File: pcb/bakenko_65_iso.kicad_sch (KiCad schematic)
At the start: 50 parts, among them J1 JST SH 4-pin, J2 Conn_01x02_MountingPin, K1 BUTTON-4P, Q1 AO3407A, U1 XC6206P302MR-G, U2 NRF52840 aQFN73, U3 MCP73831, X1 32MHz, X2 32.768KHz

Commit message: WIP + Cleaned repository
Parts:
- removed C1, C2: 1uF, Capacitor_SMD:C_0402_1005Metric, symbol Device:C_Small
- removed C11: 100pF, Capacitor_SMD:C_0402_1005Metric, symbol Device:C_Small
- removed C20: 4.7uF, Capacitor_SMD:C_0402_1005Metric, symbol Device:C_Small
- removed C7: 100nF, Capacitor_SMD:C_0402_1005Metric, symbol Device:C_Small
- removed K1: BUTTON-4P, Seeed Studio XIAO nRF52840 v1.1:SW4-SMD-2.8-2.6X1.6X0.53MM, symbol Seeed Studio XIAO nRF52840 v1.1-eagle-import:BUTTON-4P
- removed R4, R5: 33R, Resistor_SMD:R_0402_1005Metric, symbol Seeed Studio XIAO nRF52840 v1.1-eagle-import:R-0201
- added SW1: SW_Omron_B3FS, Button_Switch_SMD:SW_SPST_TS-1088-xR020, symbol Switch:SW_Omron_B3FS
- C11: renamed from C23; value 100nF -> 100pF
- C12: renamed from C29; value C_Small -> 100nF; footprint (none) -> Capacitor_SMD:C_0402_1005Metric
- C14: renamed from C31; value C_Small -> 1uF; footprint (none) -> Capacitor_SMD:C_0603_1608Metric
- C15: renamed from C27; footprint Capacitor_SMD:C_0402_1005Metric -> Capacitor_SMD:C_0603_1608Metric
- C20: renamed from C21; footprint Capacitor_SMD:C_0402_1005Metric -> Capacitor_SMD:C_0603_1608Metric
- C21: renamed from C25; footprint Capacitor_SMD:C_0402_1005Metric -> Capacitor_SMD:C_0603_1608Metric
- C6: renamed from C32; value C_Small -> 4.7uF; footprint (none) -> Capacitor_SMD:C_0603_1608Metric
- C7: renamed from C28; footprint (none) -> Capacitor_SMD:C_0402_1005Metric
- C8: renamed from C30; value C_Small -> 100nF; footprint (none) -> Capacitor_SMD:C_0402_1005Metric
- L1: renamed from C13; symbol Seeed Studio XIAO nRF52840 v1.1-eagle-import:L0201 -> Device:L
- L2: renamed from C15; symbol Seeed Studio XIAO nRF52840 v1.1-eagle-import:L0201 -> Device:L
- L3: renamed from C18; symbol Seeed Studio XIAO nRF52840 v1.1-eagle-import:L0201 -> Device:L
- R1, R10, R2, R3: symbol Seeed Studio XIAO nRF52840 v1.1-eagle-import:R-0201 -> Device:R_Small
- X1: footprint Crystal:Crystal_SMD_Abracon_ABM3C-4Pin_5.0x3.2mm -> Crystal:Crystal_SMD_2016-4Pin_2.0x1.6mm; symbol Device:Crystal_GND24_Small -> Device:Crystal
- X2: footprint Crystal:Crystal_SMD_Abracon_ABS25-4Pin_8.0x3.8mm -> Crystal:Crystal_SMD_3215-2Pin_3.2x1.5mm; symbol Device:Crystal_GND23_Small -> Device:Crystal
- renumbered C6 to C1, C12 to C10, C5 to C13, C9 to C17, C16 to C18, C8 to C2, C17 to C3, C3 to C30, C4 to C31, C14 to C33, C19 to C4, C10 to C5
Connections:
- net +3V3: now also C12.2, C14.2, C30.2, C6.2, C7.2, C8.2, R10.2, U1.2 (VO), U2.A22 (VDD), U2.AD14 (VDD), U2.AD23 (VDD), U2.B1 (VDD), U2.W1 (VDD); no longer C12.1, C14.1, C6.1, C7.1, C8.1
- net COL0: now also U2.A20 (P1.10); no longer U2.H2 (P0.27)
- net COL1: now also U2.A16 (P1.13); no longer U2.K2 (P0.05)
- net COL2: now also U2.A14 (P1.15); no longer U2.T2 (P0.11)
- net COL3: now also U2.A12 (P0.02); no longer U2.P2 (P1.08)
- net COL4: now also U2.A10 (P0.29); no longer U2.M2 (P0.07)
- net GND: now also C12.1, C14.1, C2.1, C3.1, C4.1, C6.1, C7.1, C8.1, R1.2, R12.2, U2.B3 (DCC), U3.2 (V_{SS}), SW1.2; no longer C2.2, R1.1, X1.2 (G), X1.4 (G), X2.2 (G), X2.3 (G)
- net P0.14_~{READ_BAT}: now also U2.AD10 (P0.15); no longer U2.AC9 (P0.14)
- net RESET: now also R10.1, U2.AD12 (P0.17), SW1.1; no longer R10.2
- net ROW0: now also U2.J24 (P0.10); no longer U2.U24 (P1.04)
- net ROW1: now also U2.L24 (P0.09); no longer U2.W24 (P1.02)
- net ROW3: now also U2.U24 (P1.04); no longer U2.L24 (P0.09)
- net ROW4: now also U2.W24 (P1.02); no longer U2.J24 (P0.10)
- net USB_D+: now also U2.AD6 (D+)
- net USB_D-: now also U2.AD4 (D-)
- net VBUS: now also Q1.3 (D), R1.1; no longer Q1.2 (S), R1.2
- net VIN: now also Q1.2 (S); no longer Q1.3 (D)
- net X2_P: now reaches C17.2, U2.D2 (P0.00)
- net X2_P: now also X2.2; no longer X2.4
- net XC_P: now reaches X1.1
- net XC_P: now also C2.2, U2.A23 (XC2); no longer C2.1
- net XC_N: now reaches C1.1
- net XC_N: now also U2.B24 (XC1), X1.2; no longer X1.3
- net X2_N: now reaches C18.2, U2.F2 (P0.01), X2.1
- removed net 3V3: C30.2, R10.1, U1.2 (VO)
- net P1.11_TX_D6: no longer names the net of U2.B19 (P1.11)
- no-connect marks 40 -> 27
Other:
- moved on the sheet: C1, C12, C14, C2, C5, C6, C7, C8, L1, L2, L3, Q1

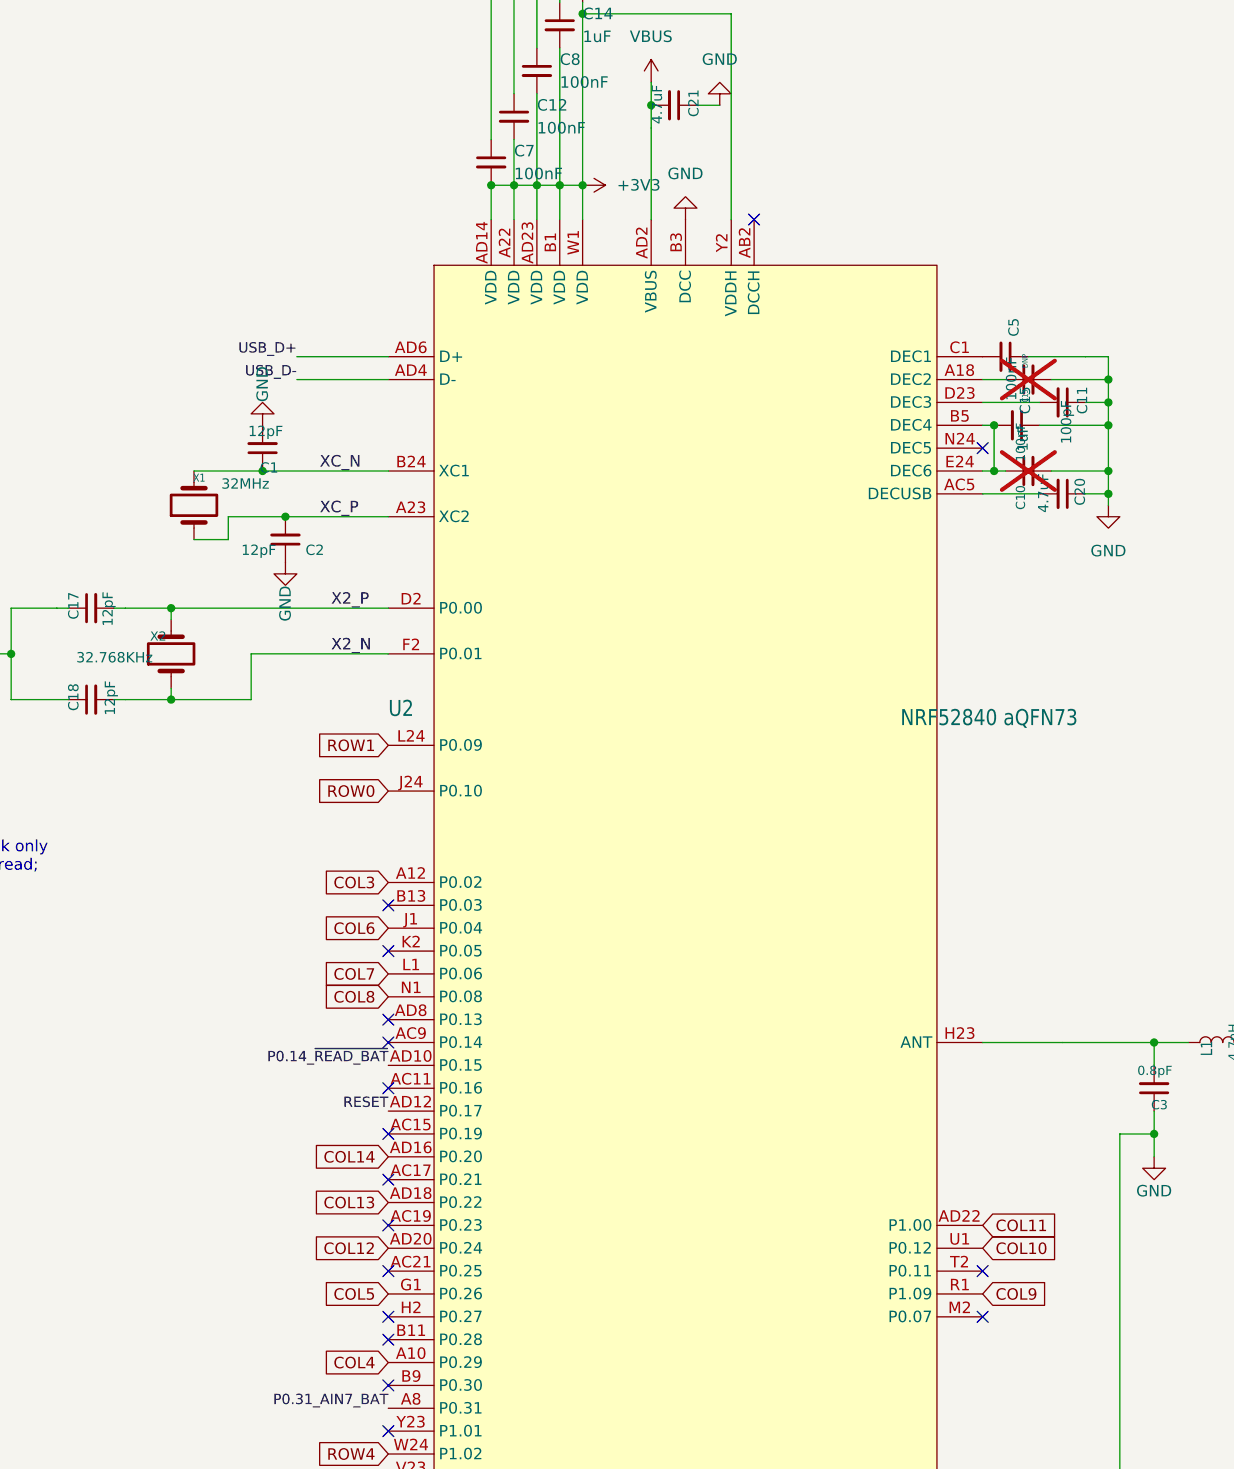
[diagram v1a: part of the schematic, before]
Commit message: 🧹Cleaned more up and updated the readme
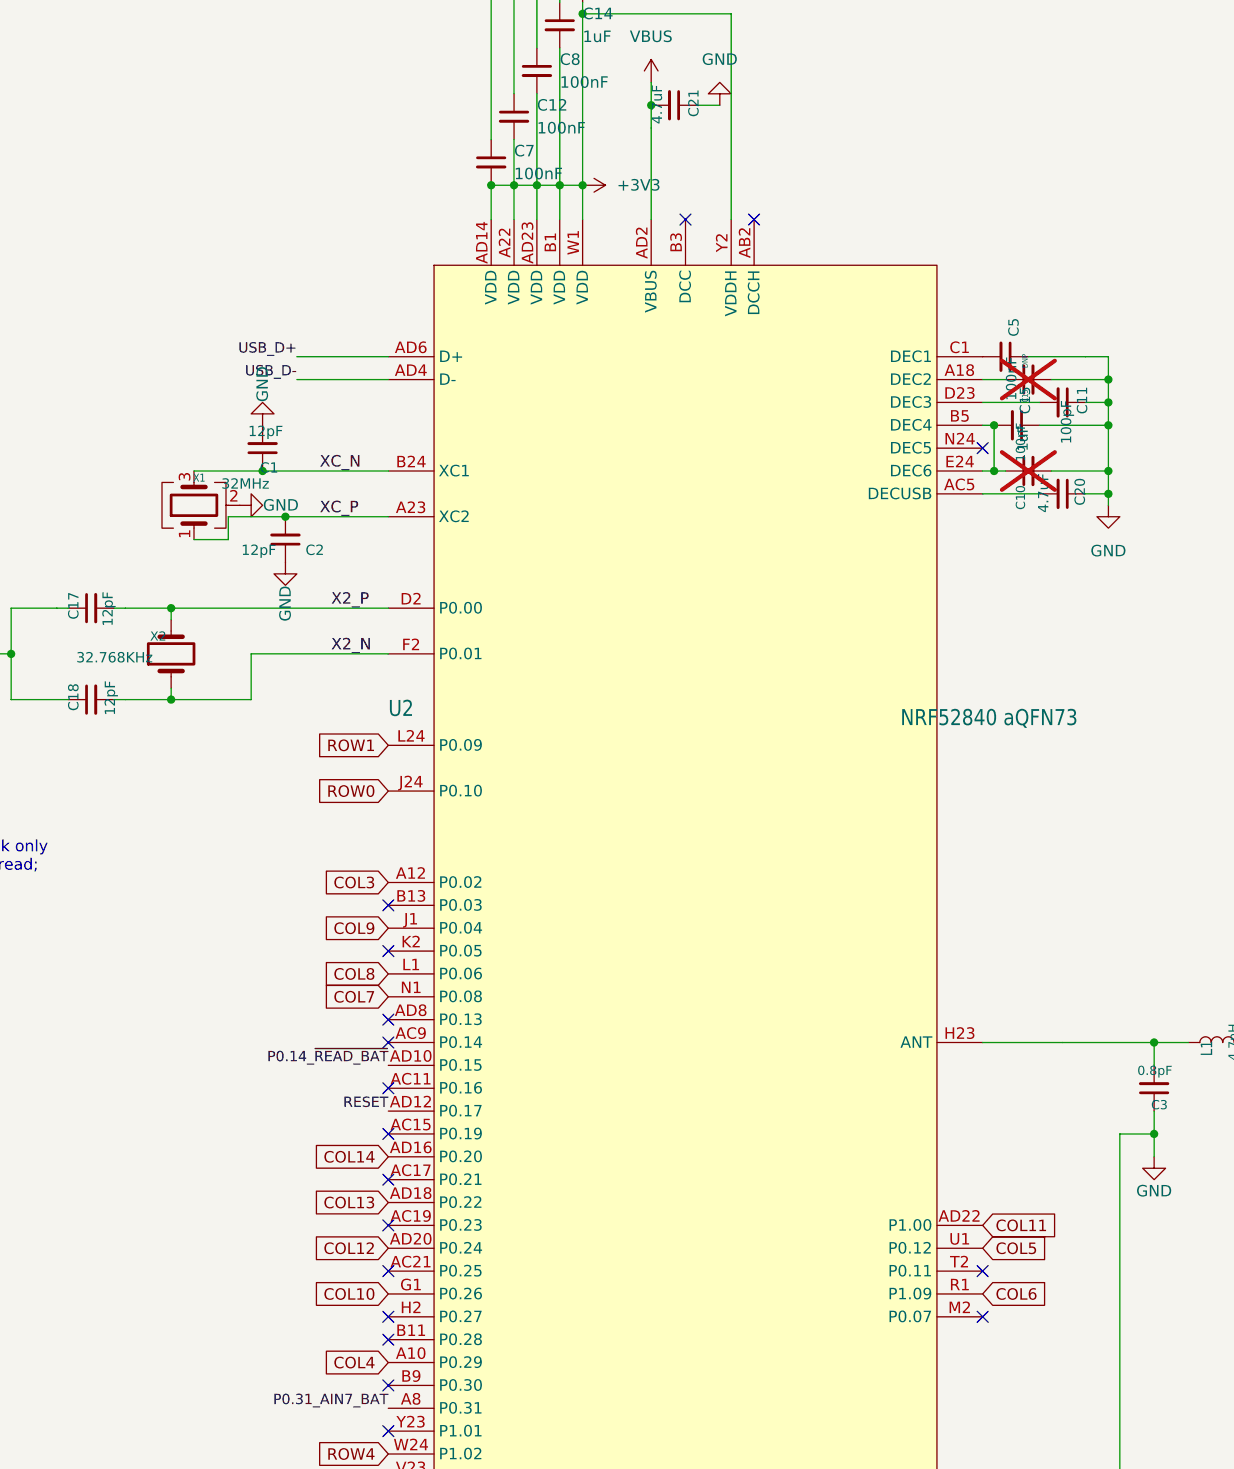
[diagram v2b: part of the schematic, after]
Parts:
- X1: symbol Device:Crystal -> Device:Crystal_GND24
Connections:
- net COL10: now also U2.G1 (P0.26); no longer U2.U1 (P0.12)
- net COL5: now also U2.U1 (P0.12); no longer U2.G1 (P0.26)
- net COL6: now also U2.R1 (P1.09); no longer U2.J1 (P0.04)
- net COL7: now also U2.N1 (P0.08); no longer U2.L1 (P0.06)
- net COL8: now also U2.L1 (P0.06); no longer U2.N1 (P0.08)
- net COL9: now also U2.J1 (P0.04); no longer U2.R1 (P1.09)
- net GND: now also X1.2 (G), X1.4 (G); no longer U2.B3 (DCC)
- net XC_N: now also X1.3; no longer X1.2
- no-connect marks 27 -> 28
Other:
- title: Bakeneko 65 V3 -> Bakeneko 65 V4 ISO
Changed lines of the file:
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@@
 	(paper "A3")
 	(title_block
-		(title "Bakeneko 65 V3")
-		(date "2020-08-01")
-		(rev "1")
-		(comment 1 "Copyright © 2020 kkatano")
-		(comment 2 "MIT License")
+		(title "Bakeneko 65 V4 ISO")
+		(date "2026-04-06")
+		(comment 1 "MIT License")
 	)
 	(text "nRF52840"
@@
 	)
 	(no_connect
+		(at 215.9 92.71)
+	)
+	(no_connect
 		(at 182.88 232.41)
 	)
@@
 		)
 	)
-	(global_label "COL9"
+	(global_label "COL6"
 		(shape input)
 		(at 248.92 212.09 0)
@@
 		)
 	)
-	(global_label "COL8"
+	(global_label "COL7"
 		(shape input)
 		(at 182.88 179.07 180)
@@
 		)
 	)
-	(global_label "COL7"
+	(global_label "COL8"
 		(shape input)
 		(at 182.88 176.53 180)
@@
 		)
 	)
-	(global_label "COL10"
+	(global_label "COL5"
 		(shape input)
 		(at 248.92 207.01 0)
@@
 		)
 	)
-	(global_label "COL6"
+	(global_label "COL9"
 		(shape input)
 		(at 182.88 171.45 180)
@@
 		)
 	)
-	(global_label "COL5"
+	(global_label "COL10"
 		(shape input)
 		(at 182.88 212.09 180)
@@
 	)
 	(symbol
+		(lib_name "GND_26")
+		(lib_id "power:GND")
+		(at 166.37 124.46 90)
+		(unit 1)
+		(body_style 1)
+		(exclude_from_sim no)
+		(in_bom yes)
+		(on_board yes)
+		(in_pos_files yes)
+		(dnp no)
+		(property "Reference" "#PWR034"
+			(at 172.72 124.46 0)
+			(hide yes)
+			(show_name no)
+			(do_not_autoplace no)
+			(effects
+				(font
+					(size 1.27 1.27)
+				)
+			)
+		)
+		(property "Value" "GND"
+			(at 170.942 124.46 90)
+			(show_name no)
+			(do_not_autoplace no)
+			(effects
+				(font
+					(size 1.27 1.27)
+				)
+			)
+		)
+		(property "Footprint" ""
+			(at 166.37 124.46 0)
+			(hide yes)
+			(show_name no)
+			(do_not_autoplace no)
+			(effects
+				(font
+					(size 1.27 1.27)
+				)
+			)
+		)
+		(property "Datasheet" ""
+			(at 166.37 124.46 0)
+			(hide yes)
+			(show_name no)
+			(do_not_autoplace no)
+			(effects
+				(font
+					(size 1.27 1.27)
+				)
+			)
+		)
+		(property "Description" "Power symbol creates a global label with name \"GND\" , ground"
+			(at 166.37 124.46 0)
+			(hide yes)
+			(show_name no)
+			(do_not_autoplace no)
+			(effects
+				(font
+					(size 1.27 1.27)
+				)
+			)
+		)
+		(pin "1"
+		)
+		(instances
+			(project "bakenko_65_iso"
+				(path "/287514b3-fc8e-4781-96ec-6e4b29b57f7d"
+					(reference "#PWR034")
+					(unit 1)
+				)
+			)
+		)
+	)
+	(symbol
 		(lib_id "Regulator_Linear:XC6206PxxxMR")
 		(at 95.25 73.66 0)
@@
 	)
 	(symbol
-		(lib_id "Device:Crystal")
+		(lib_id "Device:Crystal_GND24")
 		(at 161.29 124.46 90)
 		(unit 1)
@@
 			)
 		)
-		(property "Datasheet" ""
+		(property "Datasheet" "https://www.lcsc.com/datasheet/C187794.pdf"
 			(at 161.29 124.46 0)
 			(hide yes)
@@
 			)
 		)
-		(property "Description" "XTAL SMD 2016, 32 MHz, Cl=8 pF, Total Tol: ±40 ppm"
+		(property "Description" "Four pin crystal, GND on pins 2 and 4"
 			(at 161.29 124.46 0)
 			(hide yes)
@@
 		(pin "2"
 		)
+		(pin "4"
+		)
+		(pin "3"
+		)
 		(instances
 			(project "bakenko_65_iso"
@@
 					(unit 1)
 				)
-			)
-		)
-	)
-	(symbol
-		(lib_name "GND_2")
-		(lib_id "power:GND")
-		(at 215.9 92.71 180)
-		(unit 1)
-		(body_style 1)
-		(exclude_from_sim no)
-		(in_bom yes)
-		(on_board yes)
-		(in_pos_files yes)
-		(dnp no)
-		(fields_autoplaced yes)
-		(property "Reference" "#PWR03"
-			(at 215.9 86.36 0)
-			(hide yes)
-			(show_name no)
-			(do_not_autoplace no)
-			(effects
-				(font
-					(size 1.27 1.27)
-				)
-			)
-		)
-		(property "Value" "GND"
-			(at 215.9 87.63 0)
-			(show_name no)
-			(do_not_autoplace no)
-			(effects
-				(font
-					(size 1.27 1.27)
-				)
-			)
-		)
-		(property "Footprint" ""
-			(at 215.9 92.71 0)
-			(hide yes)
-			(show_name no)
-			(do_not_autoplace no)
-			(effects
-				(font
-					(size 1.27 1.27)
-				)
-			)
-		)
-		(property "Datasheet" ""
-			(at 215.9 92.71 0)
-			(hide yes)
-			(show_name no)
-			(do_not_autoplace no)
-			(effects
-				(font
-					(size 1.27 1.27)
-				)
-			)
-		)
-		(property "Description" "Power symbol creates a global label with name \"GND\" , ground"
-			(at 215.9 92.71 0)
-			(hide yes)
-			(show_name no)
-			(do_not_autoplace no)
-			(effects
-				(font
-					(size 1.27 1.27)
-				)
-			)
-		)
-		(pin "1"
-		)
-		(instances
-			(project "bakenko_65_iso"
-				(path "/287514b3-fc8e-4781-96ec-6e4b29b57f7d"
-					(reference "#PWR03")
-					(unit 1)
-				)

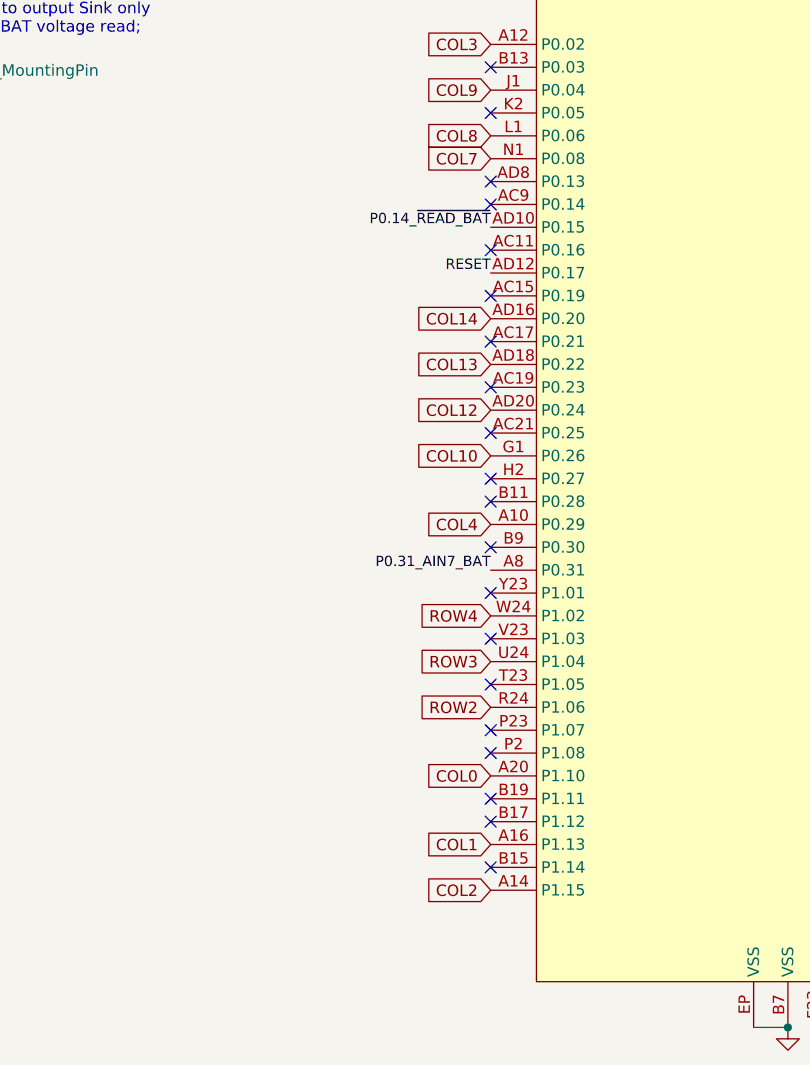
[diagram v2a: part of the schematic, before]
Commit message: Connecting reset and reducing errors and warnings
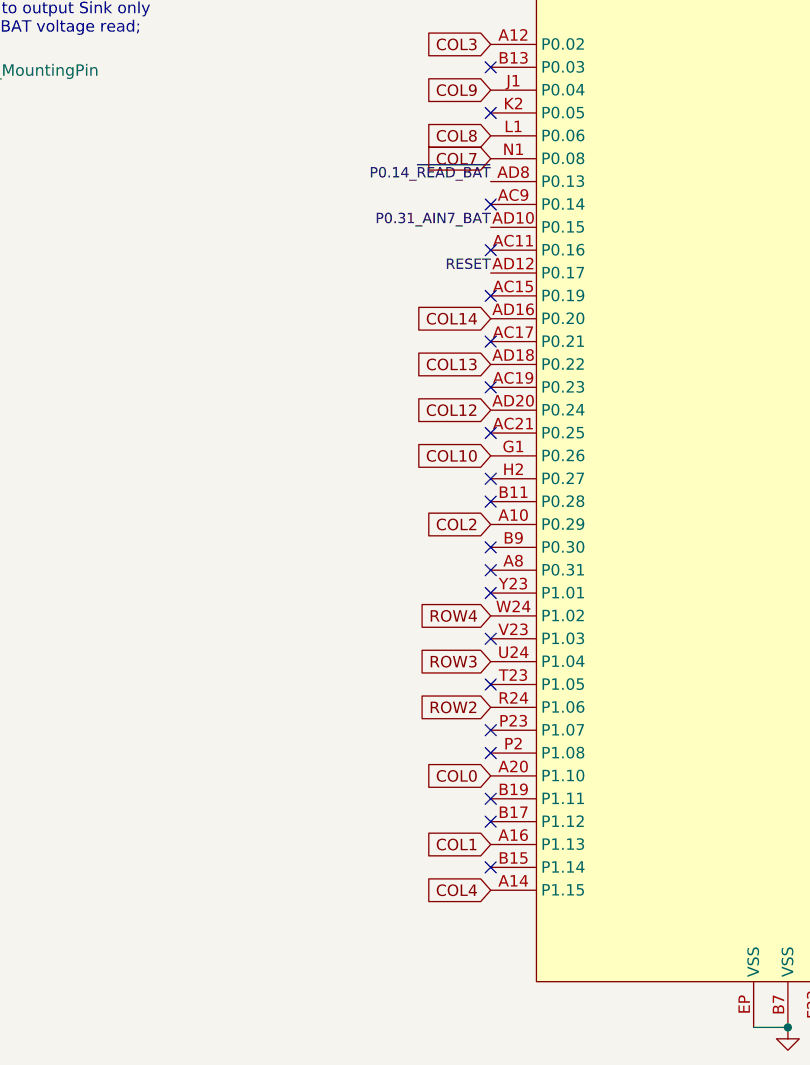
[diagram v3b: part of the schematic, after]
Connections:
- net COL2: now also U2.A10 (P0.29); no longer U2.A14 (P1.15)
- net COL4: now also U2.A14 (P1.15); no longer U2.A10 (P0.29)
- net P0.14_~{READ_BAT}: now also U2.AD8 (P0.13); no longer U2.AD10 (P0.15)
- net P0.31_AIN7_BAT: now also U2.AD10 (P0.15); no longer U2.A8 (P0.31)
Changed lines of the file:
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@@
+	)
+	(no_connect
+		(at 182.88 224.79)
 	)
 	(no_connect
@@
 	)
 	(no_connect
-		(at 182.88 181.61)
-	)
-	(no_connect
 		(at 182.88 173.99)
 	)
@@
 		)
 	)
+	(label "P0.31_AIN7_BAT"
+		(at 182.88 186.69 180)
+		(effects
+			(font
+				(size 1.143 1.143)
+			)
+			(justify right bottom)
+		)
+	)
 	(label "USB_D+"
 		(at 378.46 49.53 180)
@@
 		)
 	)
-	(label "P0.31_AIN7_BAT"
-		(at 182.88 224.79 180)
-		(effects
-			(font
-				(size 1.143 1.143)
-			)
-			(justify right bottom)
-		)
-	)
 	(label "P0.14_~{READ_BAT}"
-		(at 182.88 186.69 180)
+		(at 182.88 181.61 180)
 		(effects
 			(font
@@
 		)
 	)
-	(global_label "COL4"
+	(global_label "COL2"
 		(shape input)
 		(at 182.88 219.71 180)
@@
 		)
 	)
-	(global_label "COL2"
+	(global_label "COL4"
 		(shape input)
 		(at 182.88 260.35 180)
